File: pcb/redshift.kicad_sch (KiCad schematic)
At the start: 7 parts, among them IC1 LPC5516JEV98, J1 USB_C_Receptacle_USB2.0, SW1 SW_SPDT, SW2 SW_SPDT, SW4 SW_SPDT, U1 PMW3389DM‐T3QU

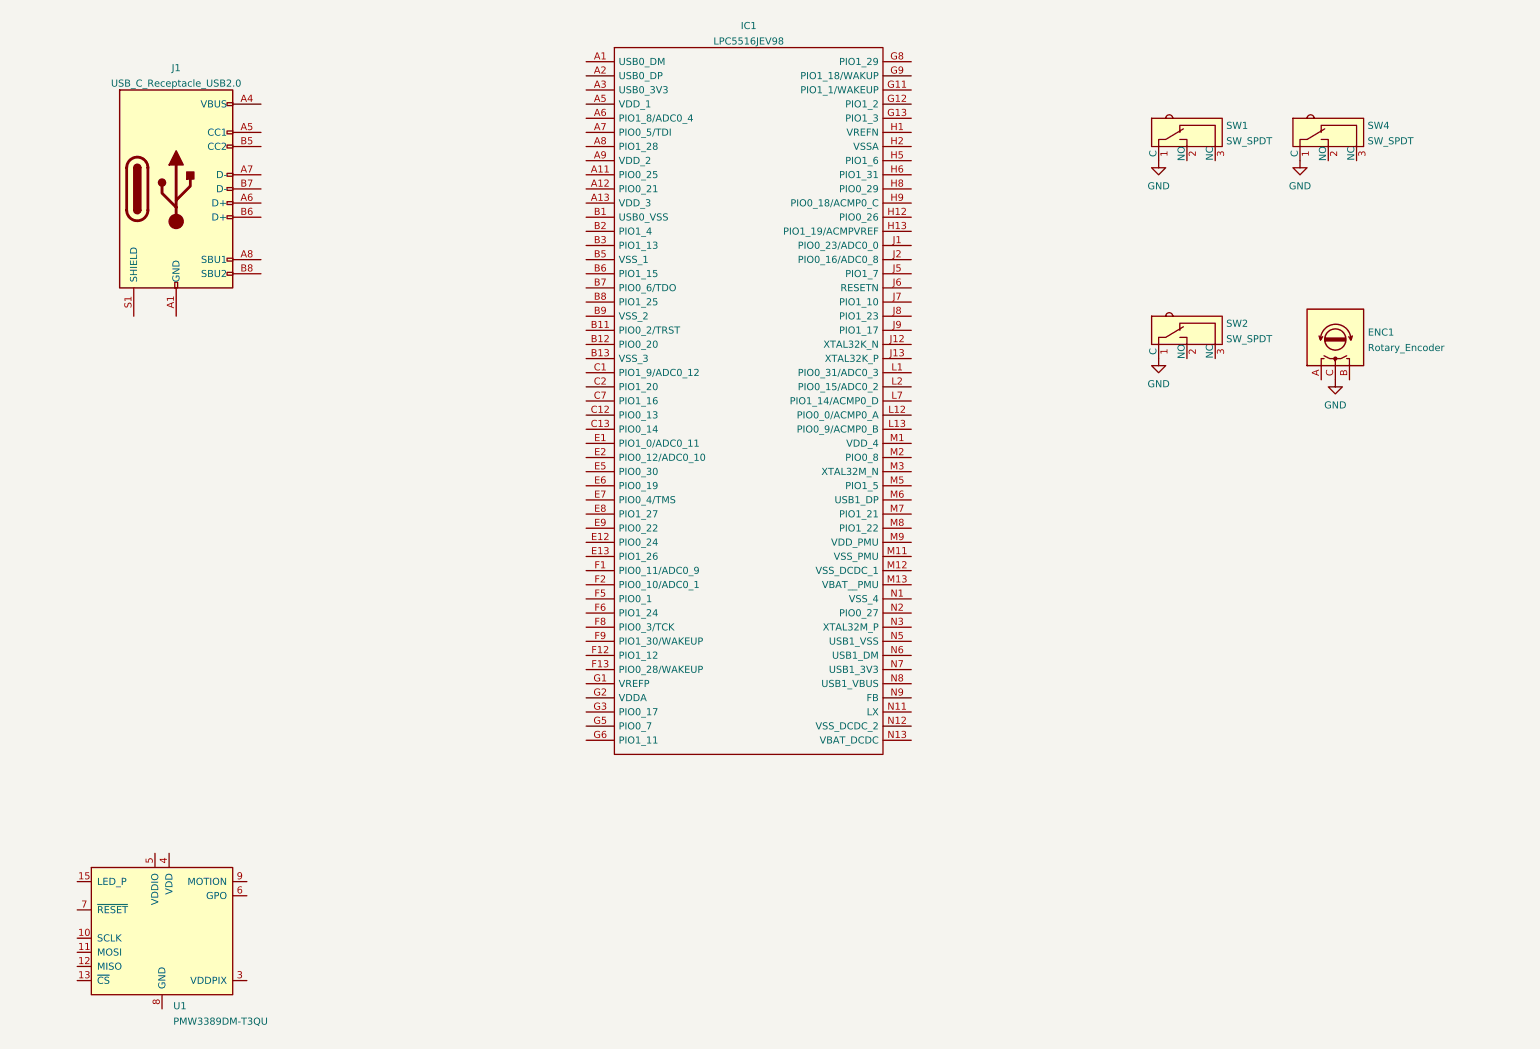
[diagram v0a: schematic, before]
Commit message: add USB and some power wires
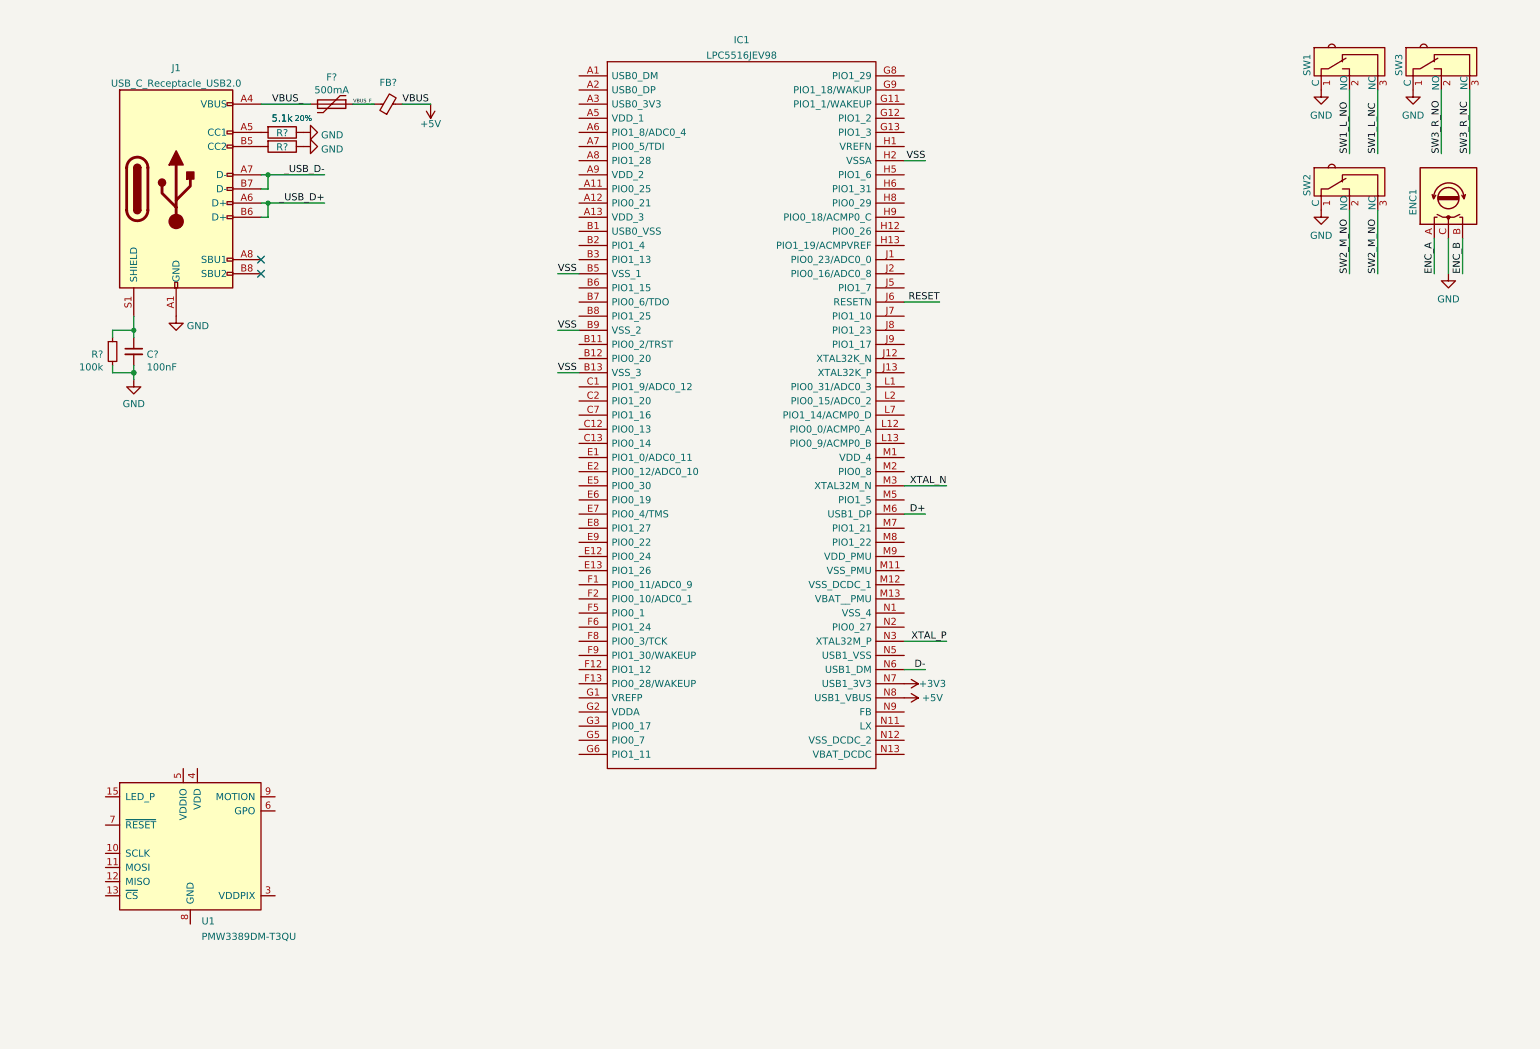
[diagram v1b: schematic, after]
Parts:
- added C?: 100nF, Capacitor_SMD:C_0402_1005Metric, symbol Device:C_Small
- added F?: 500mA, Fuse:Fuse_0603_1608Metric_Castellated, symbol Device:Polyfuse
- added FB?: ~, Inductor_SMD:L_0402_1005Metric, symbol Device:Ferrite_Bead_Small
- added R? (x2): 5.1k, Resistor_SMD:R_0402_1005Metric, symbol Device:R
- added R?: 100k, Resistor_SMD:R_0402_1005Metric, symbol Device:R_Small
- renumbered SW4 to SW3
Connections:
- net GND: now also J1.A1 (GND), J1.A12 (GND), J1.B1 (GND), J1.B12 (GND), C?.2, R?.1, R?.1, R?.2
- net ENC_A: now reaches ENC1.A
- net ENC_B: now reaches ENC1.B
- net SW1_L_NO: now reaches SW1.2 (NO)
- net SW1_L_NC: now reaches SW1.3 (NC)
- net SW3_R_NO: now reaches SW3.2 (NO)
- net SW3_R_NC: now reaches SW3.3 (NC)
- net VBUS_: now reaches J1.A4 (VBUS), J1.A9 (VBUS), J1.B4 (VBUS), J1.B9 (VBUS)
- net VBUS_: now also F?.2
- net at J1.A5 (CC1): now also R?.2
- net _USB_D+: now reaches J1.A6 (D+)
- net _USB_D+: now also J1.B6 (D+)
- net _USB_D-: now reaches J1.A7 (D-)
- net _USB_D-: now also J1.B7 (D-)
- net at J1.B5 (CC2): now also R?.2
- net at J1.S1 (SHIELD): now also C?.1, R?.1
- net SW2_M_NO: now reaches SW2.2 (NO)
- net SW2_M_NO: now also SW2.3 (NC)
- net VSS: now reaches IC1.B13 (VSS_3)
- net VSS: now also IC1.B5 (VSS_1), IC1.B9 (VSS_2), IC1.H2 (VSSA)
- net RESET: now reaches IC1.J6 (RESETN)
- net XTAL_N: now reaches IC1.M3 (XTAL32M_N)
- net D+: now reaches IC1.M6 (USB1_DP)
- net XTAL_P: now reaches IC1.N3 (XTAL32M_P)
- net D-: now reaches IC1.N6 (USB1_DM)
- net +3V3: now reaches IC1.N7 (USB1_3V3)
- net +5V: now reaches IC1.N8 (USB1_VBUS)
- net +5V: now also FB?.2
- new net VBUS_F_: F?.1, FB?.1
- no-connect marks 0 -> 2
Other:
- company: Dekanova LLC -> Dekanova LLC                                       https://github.com/Dekanova/redshift
- moved on the sheet: ENC1, IC1, SW1, SW2, SW3, U1

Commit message: route USB and power lines, fix ESD chip
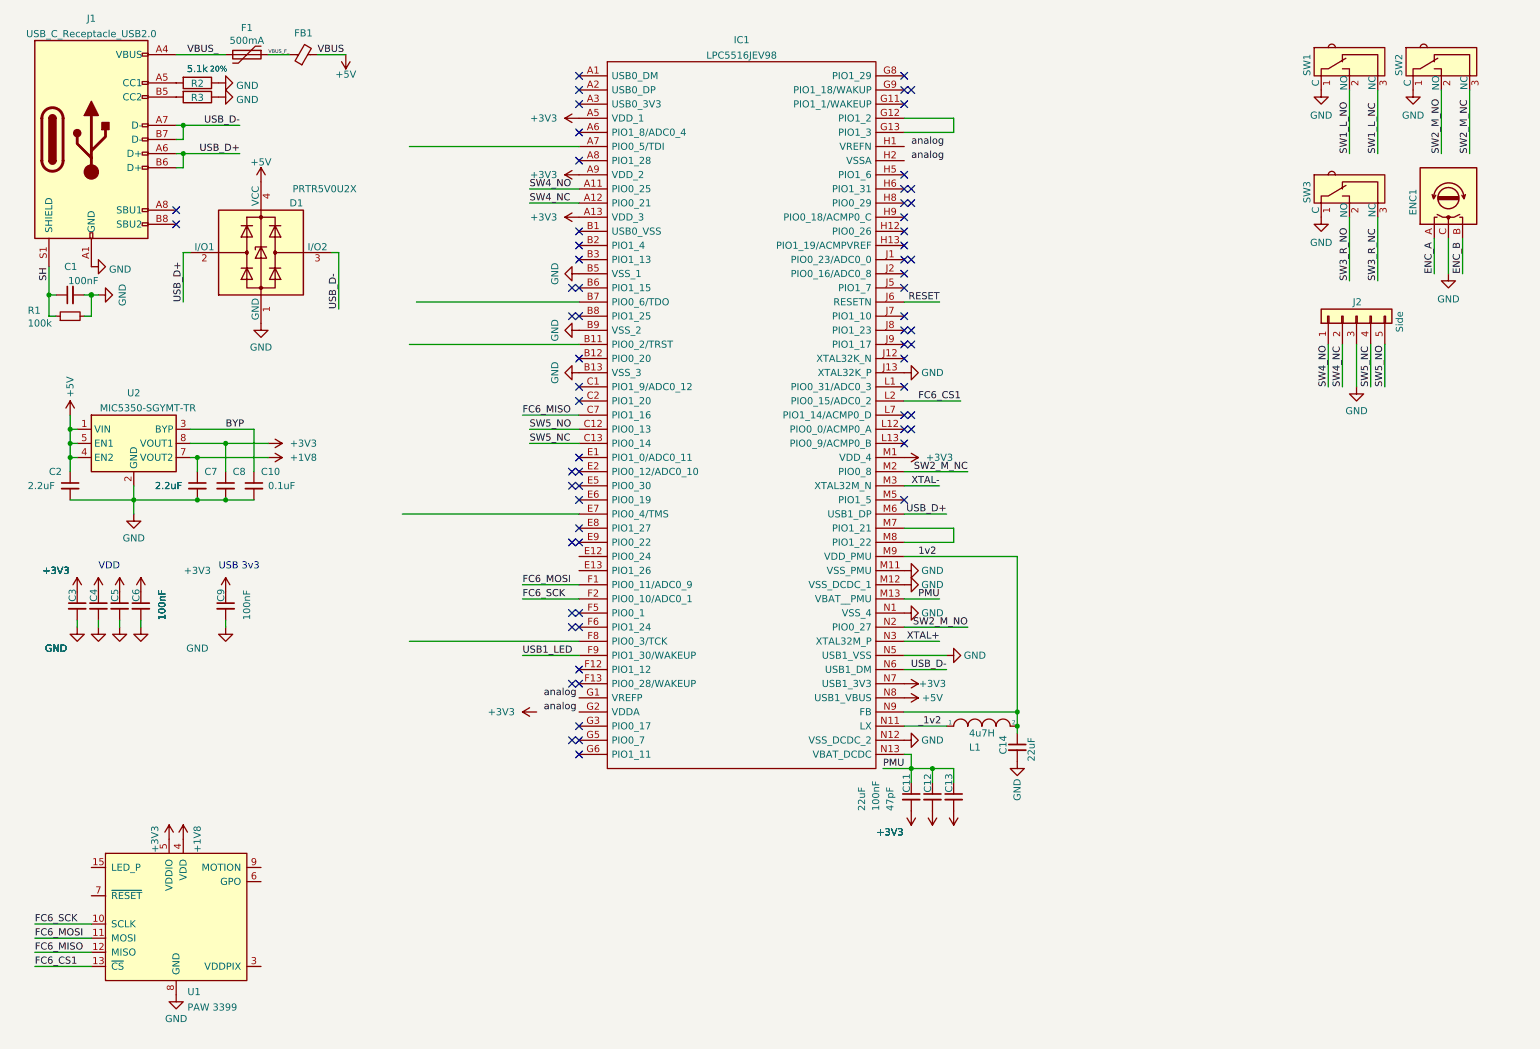
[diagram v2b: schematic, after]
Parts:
- added C10: 0.1uF, Capacitor_SMD:C_0402_1005Metric, symbol Device:C_Small
- added C11, C14: 22uF, Capacitor_SMD:C_0402_1005Metric, symbol Device:C_Small
- added C12, C3, C4, C5, C6, C9: 100nF, Capacitor_SMD:C_0402_1005Metric, symbol Device:C_Small
- added C13: 47pF, Capacitor_SMD:C_0402_1005Metric, symbol Device:C_Small
- added C2, C7, C8: 2.2uF, Capacitor_SMD:C_0402_1005Metric, symbol Device:C_Small
- added D1: PRTR5V0U2X, footprints:BF994S, symbol Power_Protection:PRTR5V0U2X
- added J2: Side, Connector_JST:JST_SH_BM05B-SRSS-TB_1x05-1MP_P1.00mm_Vertical, symbol Connector_Generic:Conn_01x05
- added L1: 4u7H, Resistor_SMD:R_0603_1608Metric, symbol pspice:INDUCTOR
- added U2: MIC5350-SGYMT-TR, Package_DFN_QFN:Micrel_MLF-8-1EP_2x2mm_P0.5mm_EP0.8x1.3mm_ThermalVias, symbol Regulator_Linear:MIC5356-SGYMME
- F1: renamed from F?; footprint Fuse:Fuse_0603_1608Metric_Castellated -> Fuse:Fuse_0402_1005Metric
- U1: value PMW3389DM‐T3QU -> PAW 3399
- gave numbers to parts that had none: 5
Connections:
- net _USB_D+ is gone; now on net USB_D+: J1.A6 (D+), J1.B6 (D+)
- net _USB_D- is gone; now on net USB_D-: J1.A7 (D-), J1.B7 (D-)
- net +3V3: now also IC1.A13 (VDD_3), IC1.A5 (VDD_1), IC1.A9 (VDD_2), IC1.M1 (VDD_4), U1.5 (VDDIO), C11.2, C12.2, C13.2, C3.1, C4.1, C5.1, C6.1, C8.1, C9.1, U2.8 (VOUT1)
- net +5V: now also C2.1, D1.4 (VCC), U2.1 (VIN), U2.4 (EN2), U2.5 (EN1)
- net GND: now also IC1.B13 (VSS_3), IC1.B5 (VSS_1), IC1.B9 (VSS_2), IC1.J13 (XTAL32K_P), IC1.M11 (VSS_PMU), IC1.M12 (VSS_DCDC_1), IC1.N1 (VSS_4), IC1.N12 (VSS_DCDC_2), IC1.N5 (USB1_VSS), U1.8 (GND), C10.2, C14.2, C2.2, C3.2, C4.2, C5.2, C6.2, C7.2, C8.2, C9.2, D1.1 (GND), J2.3 (Pin_3), U2.2 (GND), U2.9 (GND)
- net SW2_M_NO: now also IC1.N2 (PIO0_27); no longer SW2.3 (NC)
- net SH: now reaches C1.1, J1.S1 (SHIELD), R1.1
- net FC6_SCK: now reaches U1.10 (SCLK)
- net FC6_SCK: now also IC1.F2 (PIO0_10/ADC0_1)
- net FC6_MOSI: now reaches U1.11 (MOSI)
- net FC6_MOSI: now also IC1.F1 (PIO0_11/ADC0_9)
- net FC6_MISO: now reaches U1.12 (MISO)
- net FC6_MISO: now also IC1.C7 (PIO1_16)
- net FC6_CS1: now reaches U1.13 (~{CS})
- net FC6_CS1: now also IC1.L2 (PIO0_15/ADC0_2)
- net +1V8: now reaches U1.4 (VDD)
- net +1V8: now also C7.1, U2.7 (VOUT2)
- net SW4_NO: now reaches IC1.A11 (PIO0_25)
- net SW4_NO: now also J2.1 (Pin_1)
- net SW4_NC: now reaches IC1.A12 (PIO0_21)
- net SW4_NC: now also J2.2 (Pin_2)
- net SW5_NO: now reaches IC1.C12 (PIO0_13)
- net SW5_NO: now also J2.5 (Pin_5)
- net SW5_NC: now reaches IC1.C13 (PIO0_14)
- net SW5_NC: now also J2.4 (Pin_4)
- net USB1_LED: now reaches IC1.F9 (PIO1_30/WAKEUP)
- net at IC1.G12 (PIO1_2): now also IC1.G13 (PIO1_3)
- net PMU: now reaches IC1.M13 (VBAT__PMU)
- net PMU: now also IC1.N13 (VBAT_DCDC), C11.1, C12.1, C13.1
- net SW2_M_NC: now reaches IC1.M2 (PIO0_8)
- net SW2_M_NC: now also SW2.3 (NC)
- net at IC1.M7 (PIO1_21): now also IC1.M8 (PIO1_22)
- net 1v2: now reaches IC1.M9 (VDD_PMU)
- net 1v2: now also IC1.N9 (FB), C14.1, L1.2
- net _1v2: now reaches IC1.N11 (LX)
- net _1v2: now also L1.1
- net D+ renamed USB_D+
- net USB_D+: now also D1.2 (I/O1)
- net D- renamed USB_D-
- net USB_D-: now also D1.3 (I/O2)
- removed net VSS: IC1.B13 (VSS_3), IC1.B5 (VSS_1), IC1.B9 (VSS_2), IC1.H2 (VSSA)
- net XTAL_N renamed XTAL-
- net XTAL_P renamed XTAL+
- new net BYP: C10.1, U2.3 (BYP)
- no-connect marks 2 -> 66
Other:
- note added: "USB 3v3"
- note added: "VDD"
- moved on the sheet: C1, F1, FB1, J1, R1, R2, R3, SW2, SW3, U1

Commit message: add trace header and LEDs
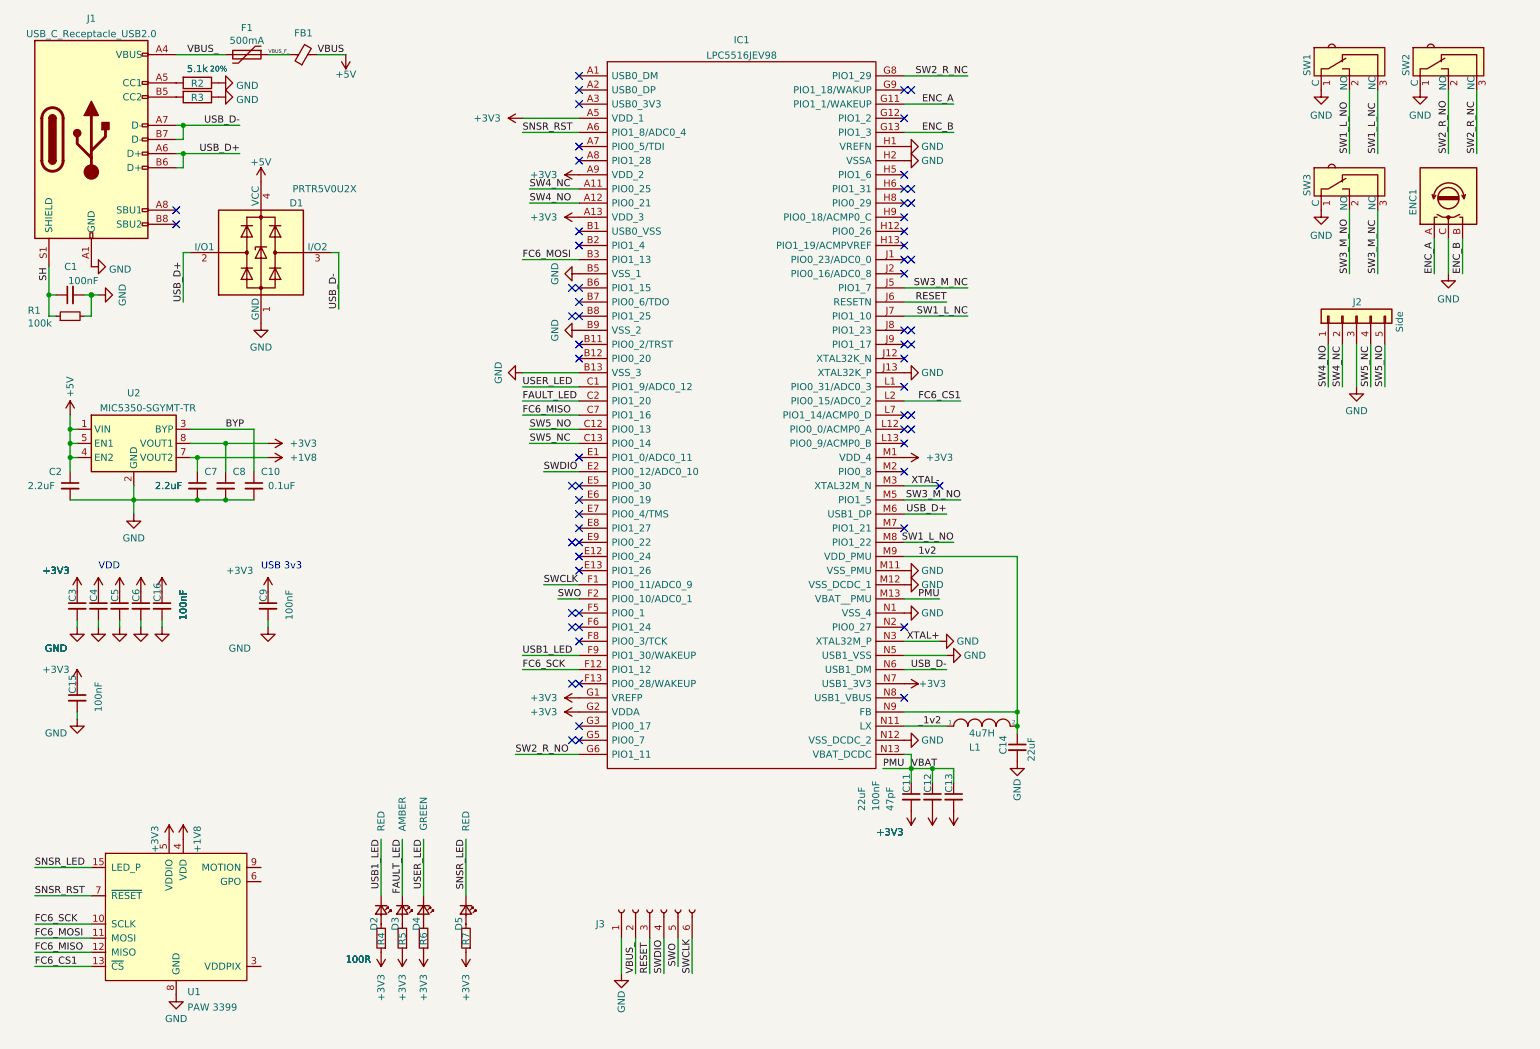
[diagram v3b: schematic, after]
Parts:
- added C15, C16: 100nF, Capacitor_SMD:C_0402_1005Metric, symbol Device:C_Small
- added D2, D5: RED, LED_SMD:LED_0402_1005Metric, symbol Device:LED_Small
- added D3: AMBER, LED_SMD:LED_0402_1005Metric, symbol Device:LED_Small
- added D4: GREEN, LED_SMD:LED_0402_1005Metric, symbol Device:LED_Small
- added J3: Conn_01x06_Female, Connector_PinHeader_2.00mm:PinHeader_1x06_P2.00mm_Vertical, symbol Connector:Conn_01x06_Female
- added R4, R5, R6, R7: 100R, Resistor_SMD:R_0402_1005Metric, symbol Device:R_Small
- ENC1: footprint (none) -> openinput:RotaryEncoder_Horizontal
- SW3: renamed from SW2; value SW_SPDT -> SW_SPD
- renumbered SW3 to SW2
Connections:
- net SW3_R_NC is gone; now on net SW2_R_NC: SW2.3 (NC)
- net SW3_R_NO is gone; now on net SW2_R_NO: SW2.2 (NO)
- net XTAL+ is gone; now on net GND: IC1.N3 (XTAL32M_P)
- net +3V3: now also IC1.G1 (VREFP), IC1.G2 (VDDA), C15.1, C16.1, R4.1, R5.1, R6.1, R7.1
- net +5V: no longer IC1.N8 (USB1_VBUS)
- net ENC_A: now also IC1.G11 (PIO1_1/WAKEUP)
- net ENC_B: now also IC1.G13 (PIO1_3)
- net FC6_MOSI: now also IC1.B3 (PIO1_13); no longer IC1.F1 (PIO0_11/ADC0_9)
- net FC6_SCK: now also IC1.F12 (PIO1_12); no longer IC1.F2 (PIO0_10/ADC0_1)
- net GND: now also IC1.H1 (VREFN), IC1.H2 (VSSA), C15.2, C16.2, J3.1 (Pin_1)
- net RESET: now also J3.3 (Pin_3)
- net SW1_L_NC: now also IC1.J7 (PIO1_10)
- net SW1_L_NO: now also IC1.M8 (PIO1_22)
- net SW4_NC: now also IC1.A11 (PIO0_25); no longer IC1.A12 (PIO0_21)
- net SW4_NO: now also IC1.A12 (PIO0_21); no longer IC1.A11 (PIO0_25)
- net USB1_LED: now also D2.1 (K)
- net VBUS_: now also J3.2 (Pin_2)
- net SNSR_LED: now reaches U1.15 (LED_P)
- net SNSR_LED: now also D5.1 (K)
- net SNSR_RST: now reaches U1.7 (~{RESET})
- net SNSR_RST: now also IC1.A6 (PIO1_8/ADC0_4)
- net USER_LED: now reaches IC1.C1 (PIO1_9/ADC0_12)
- net USER_LED: now also D4.1 (K)
- net FAULT_LED: now reaches IC1.C2 (PIO1_20)
- net FAULT_LED: now also D3.1 (K)
- net SWDIO: now reaches IC1.E2 (PIO0_12/ADC0_10)
- net SWDIO: now also J3.4 (Pin_4)
- net at IC1.G12 (PIO1_2): no longer IC1.G13 (PIO1_3)
- net SW2_R_NO: now reaches IC1.G6 (PIO1_11)
- net SW2_R_NC: now reaches IC1.G8 (PIO1_29)
- net SW3_M_NC: now reaches IC1.J5 (PIO1_7)
- net SW3_M_NC: now also SW3.3 (NC)
- net SW3_M_NO: now reaches IC1.M5 (PIO1_5)
- net SW3_M_NO: now also SW3.2 (NO)
- net at IC1.M7 (PIO1_21): no longer IC1.M8 (PIO1_22)
- net SW2_M_NC: no longer names the net of IC1.M2 (PIO0_8)
- net SW2_M_NC: no longer SW3.3 (NC)
- net SW2_M_NO: no longer names the net of IC1.N2 (PIO0_27)
- net SW2_M_NO: no longer SW3.2 (NO)
- new net: D5.2 (A), R7.2
- new net: D2.2 (A), R4.2
- new net: D3.2 (A), R5.2
- new net: D4.2 (A), R6.2
- new net SWCLK: IC1.F1 (PIO0_11/ADC0_9), J3.6 (Pin_6)
- new net SWO: IC1.F2 (PIO0_10/ADC0_1), J3.5 (Pin_5)
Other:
- moved on the sheet: C9, SW2, SW3
